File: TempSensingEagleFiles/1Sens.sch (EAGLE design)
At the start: 7 parts, among them U3 MLX90614_

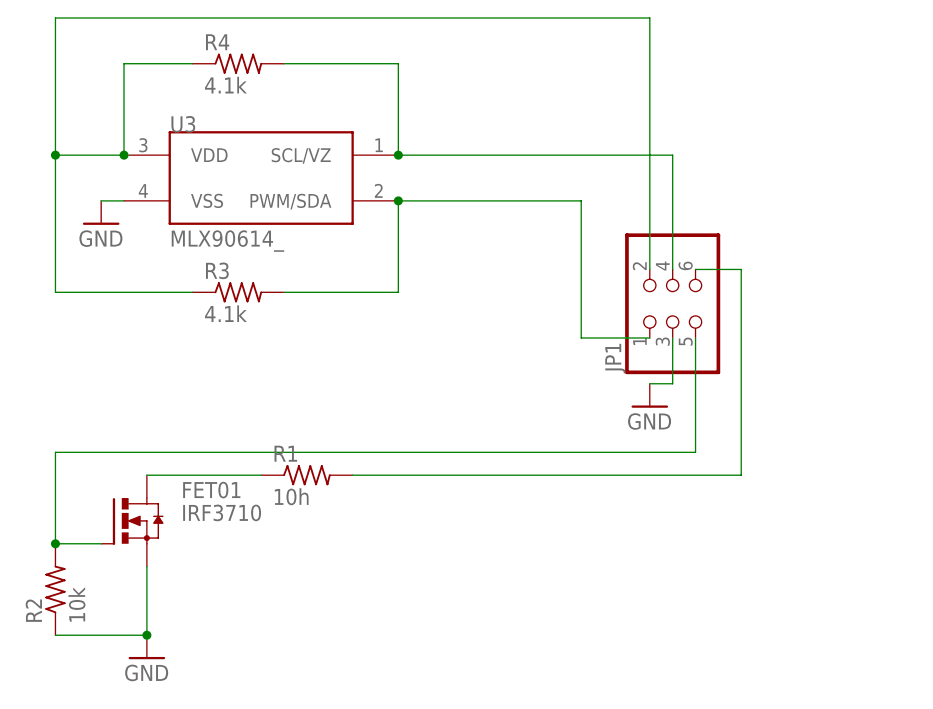
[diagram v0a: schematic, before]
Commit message: worked on Eagle Files
Added 1 Sensor and Main board
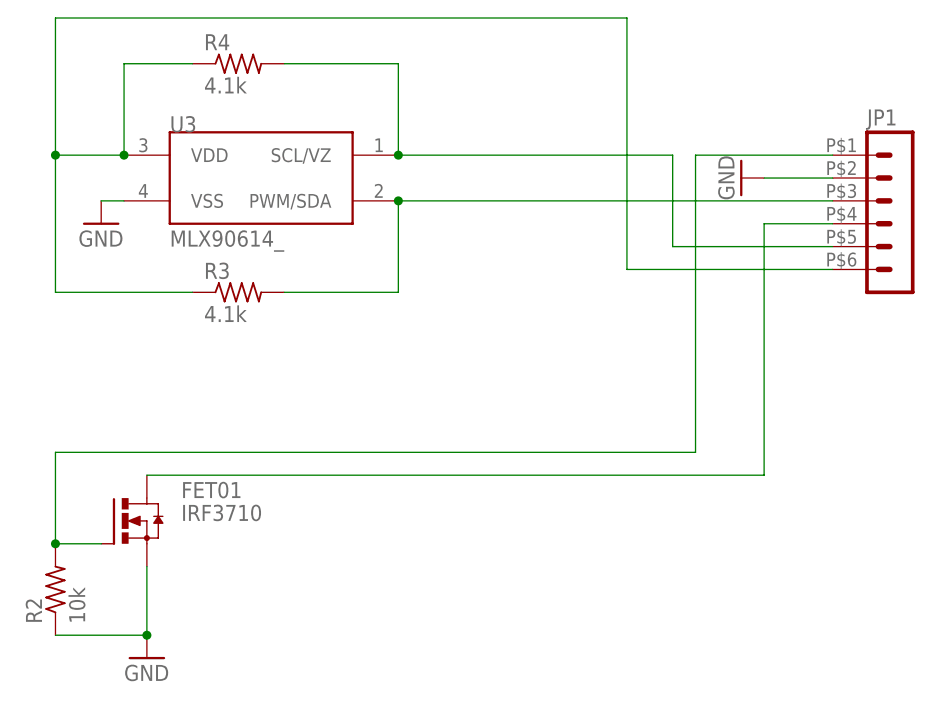
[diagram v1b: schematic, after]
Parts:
- removed R1: 10h, rcl:R-US_0207/7
- JP1: device SparkFun-Connectors:PINHD-2X3 -> con-molex-micro-fit-3_0:HEADER_POS6_43045-0600
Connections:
- removed net N$11: JP1.6, R1.2
- net GND: now also JP1.2; no longer JP1.3
- net N$1: now also JP1.6; no longer JP1.2
- net N$15: now also JP1.5; no longer JP1.4
- net N$16: now also JP1.3; no longer JP1.1
- net N$18: now also JP1.1; no longer JP1.5
- net N$2: now also JP1.4; no longer R1.1
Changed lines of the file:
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@@
 <?xml version="1.0" encoding="utf-8"?>
 <!DOCTYPE eagle SYSTEM "eagle.dtd">
-<eagle version="6.5.0">
+<eagle version="6.6.0">
 <drawing>
 <settings>
@@
 <parts>
 <part name="FET01" library="transistor-power" deviceset="IRF3704" device="" value="IRF3710"/>
-<part name="R1" library="rcl" deviceset="R-US_" device="0207/7" value="10h"/>
 <part name="R2" library="rcl" deviceset="R-US_" device="0207/7" value="10k"/>
 <part name="U3" library="SparkFun-Sensors" deviceset="MLX90614" device="_"/>
@@
 <part name="GND3" library="supply1" deviceset="GND" device=""/>
 <part name="GND4" library="supply1" deviceset="GND" device=""/>
-<part name="JP1" library="SparkFun-Connectors" deviceset="PINHD-2X3" device=""/>
+<part name="JP1" library="con-molex-micro-fit-3_0" deviceset="HEADER_POS6_?" device="43045-0600"/>
 <part name="GND5" library="supply1" deviceset="GND" device=""/>
 </parts>
@@
 <instances>
 <instance part="FET01" gate="G$1" x="139.7" y="68.58"/>
-<instance part="R1" gate="G$1" x="160.02" y="73.66"/>
 <instance part="R2" gate="G$1" x="132.08" y="60.96" rot="R90"/>
 <instance part="U3" gate="G$1" x="154.94" y="106.68"/>
@@
 <instance part="GND3" gate="1" x="142.24" y="53.34"/>
 <instance part="GND4" gate="1" x="137.16" y="101.6"/>
-<instance part="JP1" gate="A" x="200.66" y="91.44" rot="R90"/>
-<instance part="GND5" gate="1" x="198.12" y="81.28"/>
+<instance part="JP1" gate="G$1" x="223.52" y="101.6"/>
+<instance part="GND5" gate="1" x="208.28" y="106.68" rot="R270"/>
 </instances>
 <busses>
@@
 <wire x1="170.18" y1="109.22" x2="200.66" y2="109.22" width="0.1524" layer="91"/>
 <junction x="170.18" y="109.22"/>
-<pinref part="JP1" gate="A" pin="4"/>
-<wire x1="200.66" y1="96.52" x2="200.66" y2="109.22" width="0.1524" layer="91"/>
+<pinref part="JP1" gate="G$1" pin="5"/>
+<wire x1="200.66" y1="109.22" x2="200.66" y2="99.06" width="0.1524" layer="91"/>
+<wire x1="200.66" y1="99.06" x2="218.44" y2="99.06" width="0.1524" layer="91"/>
 </segment>
 </net>
@@
 <wire x1="170.18" y1="104.14" x2="170.18" y2="93.98" width="0.1524" layer="91"/>
 <wire x1="170.18" y1="93.98" x2="157.48" y2="93.98" width="0.1524" layer="91"/>
-<wire x1="170.18" y1="104.14" x2="190.5" y2="104.14" width="0.1524" layer="91"/>
-<wire x1="190.5" y1="104.14" x2="190.5" y2="88.9" width="0.1524" layer="91"/>
-<pinref part="JP1" gate="A" pin="1"/>
-<wire x1="190.5" y1="88.9" x2="198.12" y2="88.9" width="0.1524" layer="91"/>
 <junction x="170.18" y="104.14"/>
-</segment>
-</net>
-<net name="N$11" class="0">
-<segment>
-<pinref part="R1" gate="G$1" pin="2"/>
-<wire x1="165.1" y1="73.66" x2="208.28" y2="73.66" width="0.1524" layer="91"/>
-<wire x1="208.28" y1="73.66" x2="208.28" y2="96.52" width="0.1524" layer="91"/>
-<pinref part="JP1" gate="A" pin="6"/>
-<wire x1="208.28" y1="96.52" x2="203.2" y2="96.52" width="0.1524" layer="91"/>
+<pinref part="JP1" gate="G$1" pin="3"/>
+<wire x1="170.18" y1="104.14" x2="218.44" y2="104.14" width="0.1524" layer="91"/>
 </segment>
 </net>
 <net name="N$18" class="0">
 <segment>
-<pinref part="JP1" gate="A" pin="5"/>
-<wire x1="203.2" y1="88.9" x2="203.2" y2="76.2" width="0.1524" layer="91"/>
 <pinref part="FET01" gate="G$1" pin="G"/>
 <pinref part="R2" gate="G$1" pin="2"/>
@@
 <wire x1="132.08" y1="76.2" x2="132.08" y2="66.04" width="0.1524" layer="91"/>
 <junction x="132.08" y="66.04"/>
+<pinref part="JP1" gate="G$1" pin="1"/>
+<wire x1="203.2" y1="76.2" x2="203.2" y2="109.22" width="0.1524" layer="91"/>
+<wire x1="203.2" y1="109.22" x2="218.44" y2="109.22" width="0.1524" layer="91"/>
 </segment>
 </net>
@@
 <wire x1="132.08" y1="109.22" x2="132.08" y2="124.46" width="0.1524" layer="91"/>
 <junction x="132.08" y="109.22"/>
-<wire x1="132.08" y1="124.46" x2="198.12" y2="124.46" width="0.1524" layer="91"/>
-<pinref part="JP1" gate="A" pin="2"/>
-<wire x1="198.12" y1="96.52" x2="198.12" y2="124.46" width="0.1524" layer="91"/>
+<wire x1="132.08" y1="124.46" x2="195.58" y2="124.46" width="0.1524" layer="91"/>
+<pinref part="JP1" gate="G$1" pin="6"/>
+<wire x1="195.58" y1="124.46" x2="195.58" y2="96.52" width="0.1524" layer="91"/>
+<wire x1="195.58" y1="96.52" x2="218.44" y2="96.52" width="0.1524" layer="91"/>
 </segment>
 </net>
@@
 </segment>
 <segment>
-<pinref part="JP1" gate="A" pin="3"/>
 <pinref part="GND5" gate="1" pin="GND"/>
-<wire x1="200.66" y1="88.9" x2="200.66" y2="83.82" width="0.1524" layer="91"/>
-<wire x1="200.66" y1="83.82" x2="198.12" y2="83.82" width="0.1524" layer="91"/>
+<pinref part="JP1" gate="G$1" pin="2"/>
+<wire x1="210.82" y1="106.68" x2="218.44" y2="106.68" width="0.1524" layer="91"/>
 </segment>
 </net>
@@
 <segment>
 <pinref part="FET01" gate="G$1" pin="D"/>
-<pinref part="R1" gate="G$1" pin="1"/>
-<wire x1="154.94" y1="73.66" x2="142.24" y2="73.66" width="0.1524" layer="91"/>
-</segment>
-</net>
+<wire x1="142.24" y1="73.66" x2="210.82" y2="73.66" width="0.1524" layer="91"/>
+<wire x1="210.82" y1="73.66" x2="210.82" y2="101.6" width="0.1524" layer="91"/>
+<pinref part="JP1" gate="G$1" pin="4"/>
+<wire x1="210.82" y1="101.6" x2="218.44" y2="101.6" width="0.1524" layer="91"/>
+</segment>
+</net>

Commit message: STABLE: working with only one sensor
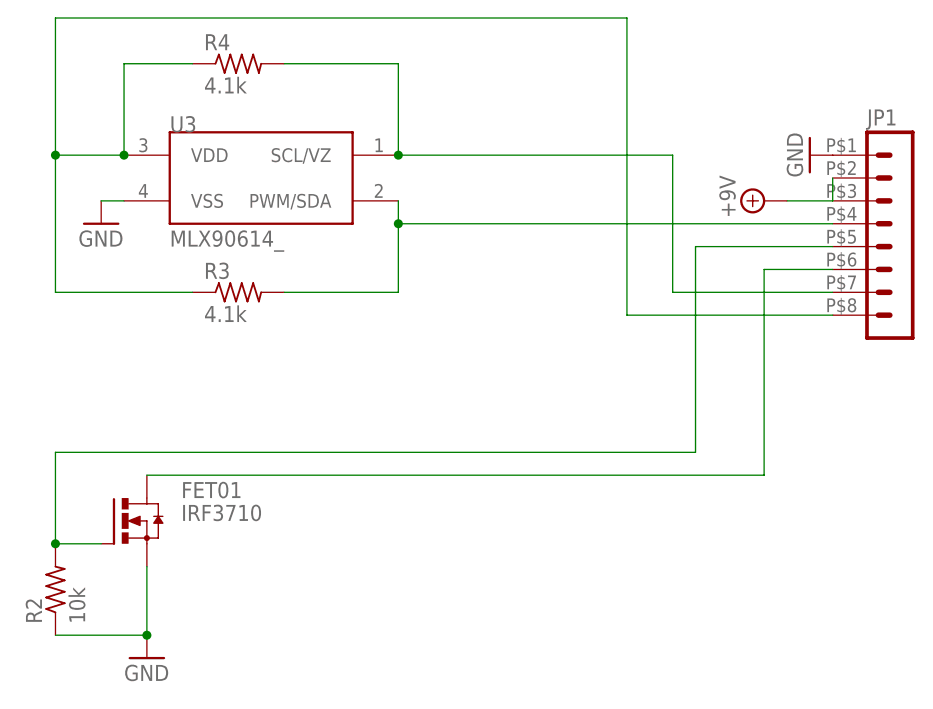
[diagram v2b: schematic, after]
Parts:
- JP1: device con-molex-micro-fit-3_0:HEADER_POS6_43045-0600 -> con-molex-micro-fit-3_0:HEADER_POS8_43045-0800
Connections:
- new net +9V: JP1.2, JP1.3
- net GND: now also JP1.1; no longer JP1.2
- net N$1: now also JP1.8; no longer JP1.6
- net N$15: now also JP1.7; no longer JP1.5
- net N$16: now also JP1.4; no longer JP1.3
- net N$18: now also JP1.5; no longer JP1.1
- net N$2: now also JP1.6; no longer JP1.4
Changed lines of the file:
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@@
 <part name="GND3" library="supply1" deviceset="GND" device=""/>
 <part name="GND4" library="supply1" deviceset="GND" device=""/>
-<part name="JP1" library="con-molex-micro-fit-3_0" deviceset="HEADER_POS6_?" device="43045-0600"/>
+<part name="JP1" library="con-molex-micro-fit-3_0" deviceset="HEADER_POS8_?" device="43045-0800"/>
 <part name="GND5" library="supply1" deviceset="GND" device=""/>
+<part name="SUPPLY1" library="supply2" deviceset="+9V" device=""/>
 </parts>
 <sheets>
@@
 <instance part="GND3" gate="1" x="142.24" y="53.34"/>
 <instance part="GND4" gate="1" x="137.16" y="101.6"/>
-<instance part="JP1" gate="G$1" x="223.52" y="101.6"/>
-<instance part="GND5" gate="1" x="208.28" y="106.68" rot="R270"/>
+<instance part="JP1" gate="G$1" x="223.52" y="99.06"/>
+<instance part="GND5" gate="1" x="215.9" y="109.22" rot="R270"/>
+<instance part="SUPPLY1" gate="G$1" x="210.82" y="104.14" rot="R90"/>
 </instances>
 <busses>
@@
 <wire x1="170.18" y1="109.22" x2="200.66" y2="109.22" width="0.1524" layer="91"/>
 <junction x="170.18" y="109.22"/>
-<pinref part="JP1" gate="G$1" pin="5"/>
-<wire x1="200.66" y1="109.22" x2="200.66" y2="99.06" width="0.1524" layer="91"/>
-<wire x1="200.66" y1="99.06" x2="218.44" y2="99.06" width="0.1524" layer="91"/>
+<wire x1="200.66" y1="109.22" x2="200.66" y2="93.98" width="0.1524" layer="91"/>
+<pinref part="JP1" gate="G$1" pin="7"/>
+<wire x1="218.44" y1="93.98" x2="200.66" y2="93.98" width="0.1524" layer="91"/>
 </segment>
 </net>
@@
 <pinref part="U3" gate="G$1" pin="PWM/SDA"/>
 <pinref part="R3" gate="G$1" pin="2"/>
-<wire x1="170.18" y1="104.14" x2="170.18" y2="93.98" width="0.1524" layer="91"/>
+<wire x1="170.18" y1="104.14" x2="170.18" y2="101.6" width="0.1524" layer="91"/>
+<wire x1="170.18" y1="101.6" x2="170.18" y2="93.98" width="0.1524" layer="91"/>
 <wire x1="170.18" y1="93.98" x2="157.48" y2="93.98" width="0.1524" layer="91"/>
-<junction x="170.18" y="104.14"/>
-<pinref part="JP1" gate="G$1" pin="3"/>
-<wire x1="170.18" y1="104.14" x2="218.44" y2="104.14" width="0.1524" layer="91"/>
+<pinref part="JP1" gate="G$1" pin="4"/>
+<wire x1="218.44" y1="101.6" x2="170.18" y2="101.6" width="0.1524" layer="91"/>
+<junction x="170.18" y="101.6"/>
 </segment>
 </net>
@@
 <wire x1="132.08" y1="76.2" x2="132.08" y2="66.04" width="0.1524" layer="91"/>
 <junction x="132.08" y="66.04"/>
-<pinref part="JP1" gate="G$1" pin="1"/>
-<wire x1="203.2" y1="76.2" x2="203.2" y2="109.22" width="0.1524" layer="91"/>
-<wire x1="203.2" y1="109.22" x2="218.44" y2="109.22" width="0.1524" layer="91"/>
+<pinref part="JP1" gate="G$1" pin="5"/>
+<wire x1="218.44" y1="99.06" x2="203.2" y2="99.06" width="0.1524" layer="91"/>
+<wire x1="203.2" y1="99.06" x2="203.2" y2="76.2" width="0.1524" layer="91"/>
 </segment>
 </net>
@@
 <junction x="132.08" y="109.22"/>
 <wire x1="132.08" y1="124.46" x2="195.58" y2="124.46" width="0.1524" layer="91"/>
-<pinref part="JP1" gate="G$1" pin="6"/>
-<wire x1="195.58" y1="124.46" x2="195.58" y2="96.52" width="0.1524" layer="91"/>
-<wire x1="195.58" y1="96.52" x2="218.44" y2="96.52" width="0.1524" layer="91"/>
+<wire x1="195.58" y1="124.46" x2="195.58" y2="91.44" width="0.1524" layer="91"/>
+<pinref part="JP1" gate="G$1" pin="8"/>
+<wire x1="218.44" y1="91.44" x2="195.58" y2="91.44" width="0.1524" layer="91"/>
 </segment>
 </net>
@@
 </segment>
 <segment>
+<pinref part="JP1" gate="G$1" pin="1"/>
 <pinref part="GND5" gate="1" pin="GND"/>
-<pinref part="JP1" gate="G$1" pin="2"/>
-<wire x1="210.82" y1="106.68" x2="218.44" y2="106.68" width="0.1524" layer="91"/>
 </segment>
 </net>
@@
 <pinref part="FET01" gate="G$1" pin="D"/>
 <wire x1="142.24" y1="73.66" x2="210.82" y2="73.66" width="0.1524" layer="91"/>
-<wire x1="210.82" y1="73.66" x2="210.82" y2="101.6" width="0.1524" layer="91"/>
-<pinref part="JP1" gate="G$1" pin="4"/>
-<wire x1="210.82" y1="101.6" x2="218.44" y2="101.6" width="0.1524" layer="91"/>
+<pinref part="JP1" gate="G$1" pin="6"/>
+<wire x1="218.44" y1="96.52" x2="210.82" y2="96.52" width="0.1524" layer="91"/>
+<wire x1="210.82" y1="96.52" x2="210.82" y2="73.66" width="0.1524" layer="91"/>
 </segment>
 </net>
+<net name="+9V" class="0">
+<segment>
+<pinref part="JP1" gate="G$1" pin="3"/>
+<pinref part="SUPPLY1" gate="G$1" pin="+9V"/>
+<wire x1="213.36" y1="104.14" x2="218.44" y2="104.14" width="0.1524" layer="91"/>
+<pinref part="JP1" gate="G$1" pin="2"/>
+<wire x1="218.44" y1="106.68" x2="218.44" y2="104.14" width="0.1524" layer="91"/>
+</segment>
+</net>
